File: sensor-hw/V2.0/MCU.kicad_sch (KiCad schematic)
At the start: 35 parts, among them SW1 SW_MEC_5E, U2 STM32WL55JCI7, x2 NX2012SA 32.768KHz

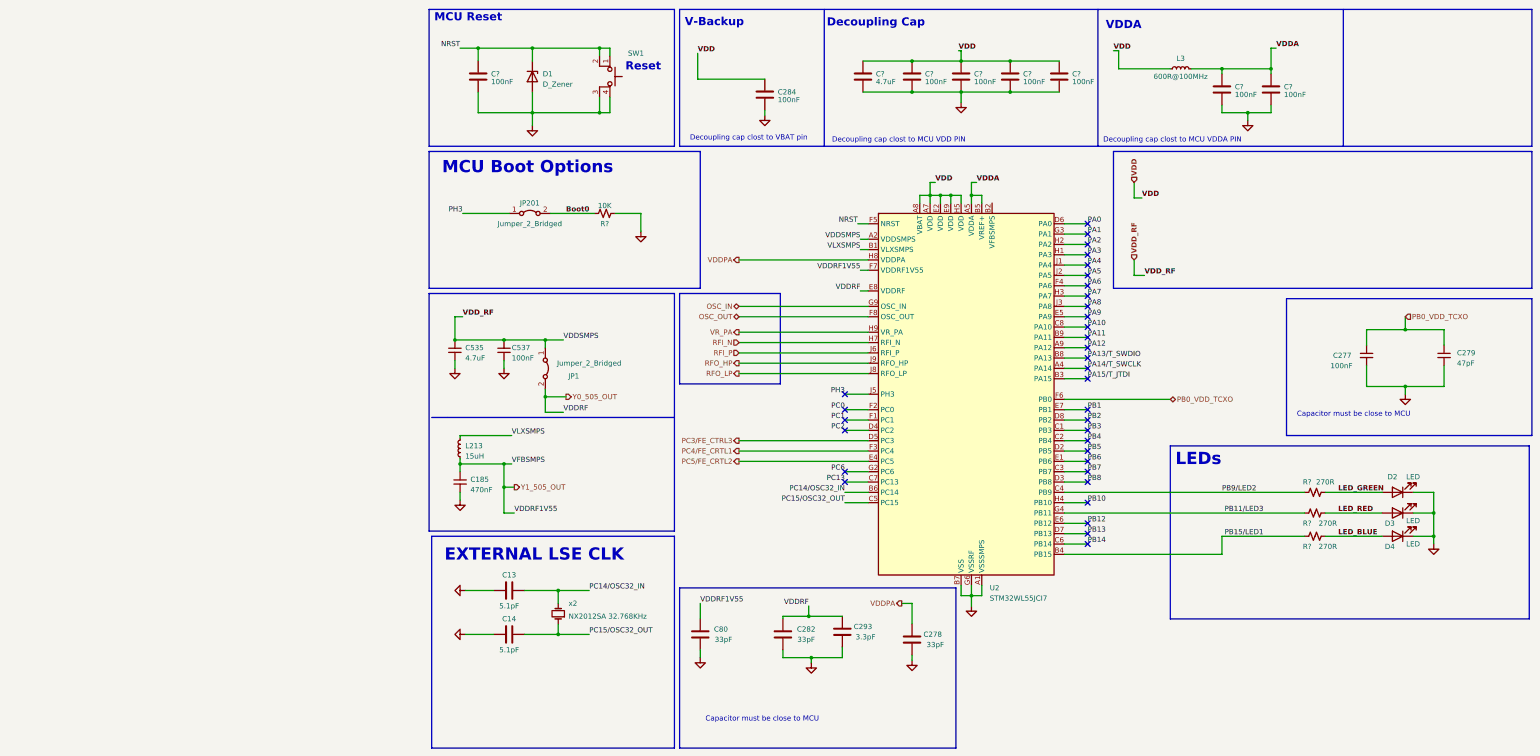
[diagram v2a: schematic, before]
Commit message: updated components fields and footprint in MCU page
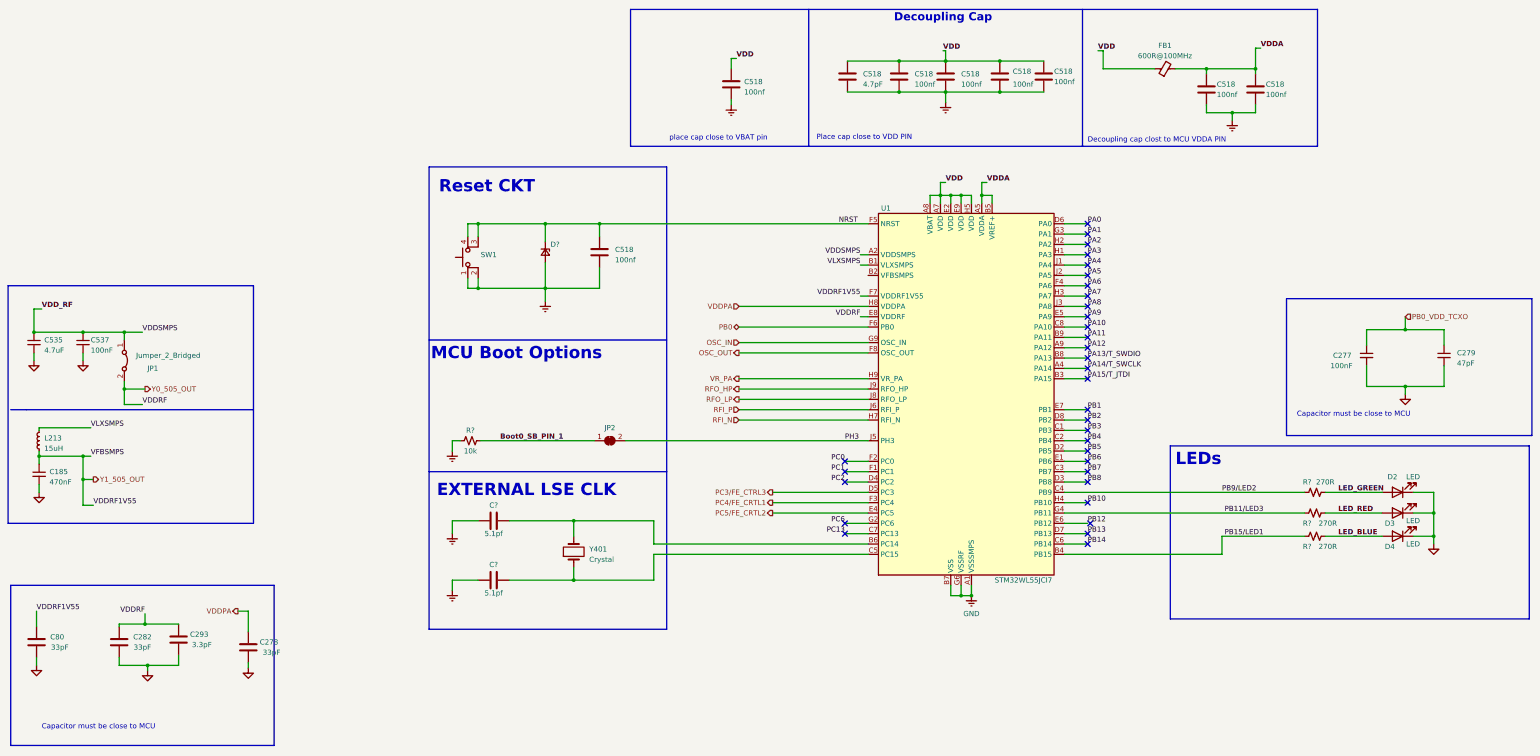
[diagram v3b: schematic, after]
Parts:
- removed C13, C14: 5.1pF, symbol Device:C
- removed C284, C? (x7): 100nF, symbol Device:C
- removed C?: 4.7uF, symbol Device:C
- removed D1: D_Zener, symbol Device:D_Zener
- removed JP201: Jumper_2_Bridged, symbol Jumper:Jumper_2_Bridged
- removed L3: 600R@100MHz, symbol Device:L_Small
- removed R?: 10K, symbol Device:R_Small_US
- removed SW1: SW_MEC_5E, symbol Switch:SW_MEC_5E
- removed U2: STM32WL55JCI7, Package_BGA:ST_UFBGA-73_5x5mm_Layout9x9_P0.5mm, symbol MCU_ST_STM32WL:STM32WLE5JCIx
- removed x2: NX2012SA 32.768KHz, symbol Device:Crystal_Small
- added C518 (x8): 100nf, Capacitor_SMD:C_0603_1608Metric_Pad1.08x0.95mm_HandSolder, symbol Local:Capcitor
- added C518: 4.7pF, Capacitor_SMD:C_0603_1608Metric_Pad1.08x0.95mm_HandSolder, symbol Local:Capcitor
- added C? (x2): 5.1pf, Local:Cap_0603_1608Metric_Pad1.08x0.95mm_HandSolder, symbol Local:Capacitor
- added D?: D_Zener_Small, Local:D_0201_0603Metric_Pad0.64x0.40mm_HandSolder, symbol Local:ESD_Zener
- added FB1: 600R@100MHz, Local:L_0603_1608Metric_Pad1.05x0.95mm, symbol Local:FerriteBead
- added JP2: SolderBridge_close, Local:SolderJumper-close-2_P1.3mm_Bridged_Pad1.0x1.5mm, symbol Local:SolderBridge_close
- added R?: 10k, Local:R_0603_1608Metric_Pad0.98x0.95mm_HandSolder, symbol Local:R
- added SW1: SW_MEC_5E, Local:SW_Push_1P1T-SH_NO_CK_KMR231GLFS, symbol Local:SW_MEC
- added U1: STM32WL55JCI7, Local:ST_UFBGA-73_5x5mm_Layout9x9_P0.5mm, symbol Local:STM32WL55JCI7
- added Y401: Crystal, Local:XTAL_NX2012SA-32.768K-STD-MUB-1, symbol Local:Crystal
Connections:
- net NRST: now also C518.1, D?.1 (K), SW1.3 (K), SW1.4 (A), U1.F5 (NRST)
- net OSC_IN: now also U1.G9 (OSC_IN)
- net OSC_OUT: now also U1.F8 (OSC_OUT)
- net PA0: now also U1.D6 (PA0)
- net PA1: now also U1.G3 (PA1)
- net PA10: now also U1.C8 (PA10)
- net PA11: now also U1.B9 (PA11)
- net PA12: now also U1.A9 (PA12)
- net PA13/T_SWDIO: now also U1.B8 (PA13)
- net PA14/T_SWCLK: now also U1.A4 (PA14)
- net PA15/T_JTDI: now also U1.B3 (PA15)
- net PA2: now also U1.H2 (PA2)
- net PA3: now also U1.H1 (PA3)
- net PA4: now also U1.J1 (PA4)
- net PA5: now also U1.J2 (PA5)
- net PA6: now also U1.F4 (PA6)
- net PA7: now also U1.H3 (PA7)
- net PA8: now also U1.J3 (PA8)
- net PA9: now also U1.E5 (PA9)
- net PB1: now also U1.E7 (PB1)
- net PB10: now also U1.H4 (PB10)
- net PB11/LED3: now also U1.G4 (PB11)
- net PB12: now also U1.E6 (PB12)
- net PB13: now also U1.D7 (PB13)
- net PB14: now also U1.C6 (PB14)
- net PB15/LED1: now also U1.B4 (PB15)
- net PB2: now also U1.D8 (PB2)
- net PB3: now also U1.C1 (PB3)
- net PB4: now also U1.C2 (PB4)
- net PB5: now also U1.D2 (PB5)
- net PB6: now also U1.E1 (PB6)
- net PB7: now also U1.C3 (PB7)
- net PB8: now also U1.D3 (PB8)
- net PB9/LED2: now also U1.C4 (PB9)
- net PC0: now also U1.F2 (PC0)
- net PC1: now also U1.F1 (PC1)
- net PC13: now also U1.C7 (PC13)
- net PC2: now also U1.D4 (PC2)
- net PC3/FE_CTRL3: now also U1.D5 (PC3)
- net PC4/FE_CRTL1: now also U1.F3 (PC4)
- net PC5/FE_CRTL2: now also U1.E4 (PC5)
- net PC6: now also U1.G2 (PC6)
- net PH3: now also JP2.2 (B), U1.J5 (PH3)
- net RFI_N: now also U1.H7 (RFI_N)
- net RFI_P: now also U1.J6 (RFI_P)
- net RFO_HP: now also U1.J9 (RFO_HP)
- net RFO_LP: now also U1.J8 (RFO_LP)
- net VDD: now also C518.1, C518.1, C518.1, C518.1, C518.1, C518.1, FB1.1, U1.A7 (VDD), U1.A8 (VBAT), U1.E2 (VDD), U1.E9 (VDD), U1.H5 (VDD)
- net VDDA: now also C518.1, C518.1, FB1.2, U1.A5 (VDDA), U1.B5 (VREF+)
- net VDDPA: now also U1.H8 (VDDPA)
- net VLXSMPS: now also U1.B1 (VLXSMPS)
- net VR_PA: now also U1.H9 (VR_PA)
- net Y0_505_OUT: now also U1.E8 (VDDRF)
- net Y1_505_OUT: now also U1.F7 (VDDRF1V55)
- net VDD_RF renamed VDDSMPS
- net VDDSMPS: now also U1.A2 (VDDSMPS)
- new net: C?.2, U1.C5 (PC15), Y401.1
- new net: C?.2, U1.B6 (PC14), Y401.2
- new net Boot0_SB_PIN_1: JP2.1 (A), R?.2
- new net GNDREF: C518.2, C518.2, C518.2, C518.2, C518.2, C518.2, C518.2, C518.2, C518.2, C?.1, C?.1, D?.2 (A), R?.1, SW1.1, SW1.2, U1.A1 (VSSSMPS), U1.B7 (VSS), U1.D9 (VSS), U1.E3 (VSS), U1.G5 (VSS), U1.G6 (VSSRF), U1.G7 (VSSRF), U1.G8 (VSSRF), U1.H6 (VSSRF)
- new net PB0: U1.F6 (PB0)
- no-connect marks 34 -> 33
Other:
- note added: "Place cap close to VDD PIN"
- note added: "Reset CKT"
- note added: "place cap close to VBAT pin"
- note removed: "Decoupling cap clost to MCU VDD PIN"
- note removed: "Decoupling cap clost to VBAT pin"
- note removed: "MCU Reset"
- note removed: "Reset"
- note removed: "V-Backup"
- note removed: "VDDA"
- moved on the sheet: C185, C278, C282, C293, C535, C537, C80, JP1, L213
